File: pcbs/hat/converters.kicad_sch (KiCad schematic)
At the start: 7 parts, among them U18 MCP3008, U19 MCP3008, U20 MCP3008, U21 ???

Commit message: more work on charging circuit
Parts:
- renumbered C25 to C41, C26 to C42, R33 to R65
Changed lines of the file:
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@@
   (symbol (lib_id "power:+5V") (at 90.17 96.52 0) (unit 1)
     (in_bom yes) (on_board yes)
-    (property "Reference" "#PWR0195" (id 0) (at 90.17 100.33 0)
+    (property "Reference" "#PWR0142" (id 0) (at 90.17 100.33 0)
       (effects (font (size 1.27 1.27)) hide)
     )
@@
   (symbol (lib_id "power:GND") (at 86.36 124.46 0) (unit 1)
     (in_bom yes) (on_board yes)
-    (property "Reference" "#PWR0135" (id 0) (at 86.36 130.81 0)
+    (property "Reference" "#PWR0139" (id 0) (at 86.36 130.81 0)
       (effects (font (size 1.27 1.27)) hide)
     )
@@
   (symbol (lib_id "power:+5VA") (at 82.55 52.07 0) (unit 1)
     (in_bom yes) (on_board yes)
-    (property "Reference" "#PWR0159" (id 0) (at 82.55 55.88 0)
+    (property "Reference" "#PWR0135" (id 0) (at 82.55 55.88 0)
       (effects (font (size 1.27 1.27)) hide)
     )
@@
   (symbol (lib_id "power:+5V") (at 90.17 140.97 0) (unit 1)
     (in_bom yes) (on_board yes)
-    (property "Reference" "#PWR0147" (id 0) (at 90.17 144.78 0)
+    (property "Reference" "#PWR0143" (id 0) (at 90.17 144.78 0)
       (effects (font (size 1.27 1.27)) hide)
     )
@@
   (symbol (lib_id "power:GND") (at 86.36 168.91 0) (unit 1)
     (in_bom yes) (on_board yes) (fields_autoplaced)
-    (property "Reference" "#PWR0111" (id 0) (at 86.36 175.26 0)
+    (property "Reference" "#PWR0140" (id 0) (at 86.36 175.26 0)
       (effects (font (size 1.27 1.27)) hide)
     )
@@
   (symbol (lib_id "Device:R") (at 200.025 53.34 90) (unit 1)
     (in_bom yes) (on_board yes) (fields_autoplaced)
-    (property "Reference" "R33" (id 0) (at 200.025 46.99 90))
+    (property "Reference" "R65" (id 0) (at 200.025 46.99 90))
     (property "Value" "R" (id 1) (at 200.025 49.53 90))
     (property "Footprint" "" (id 2) (at 200.025 55.118 90)
@@
   (symbol (lib_id "power:GND") (at 86.36 80.01 0) (unit 1)
     (in_bom yes) (on_board yes) (fields_autoplaced)
-    (property "Reference" "#PWR0203" (id 0) (at 86.36 86.36 0)
+    (property "Reference" "#PWR0138" (id 0) (at 86.36 86.36 0)
       (effects (font (size 1.27 1.27)) hide)
     )
@@
   (symbol (lib_id "power:+5VA") (at 82.55 140.97 0) (unit 1)
     (in_bom yes) (on_board yes)
-    (property "Reference" "#PWR0123" (id 0) (at 82.55 144.78 0)
+    (property "Reference" "#PWR0137" (id 0) (at 82.55 144.78 0)
       (effects (font (size 1.27 1.27)) hide)
     )
@@
   (symbol (lib_id "Device:C") (at 210.185 60.96 0) (unit 1)
     (in_bom yes) (on_board yes) (fields_autoplaced)
-    (property "Reference" "C25" (id 0) (at 213.995 59.6899 0)
+    (property "Reference" "C41" (id 0) (at 213.995 59.6899 0)
       (effects (font (size 1.27 1.27)) (justify left))
     )
@@
   (symbol (lib_id "power:+5VA") (at 82.55 96.52 0) (unit 1)
     (in_bom yes) (on_board yes)
-    (property "Reference" "#PWR0183" (id 0) (at 82.55 100.33 0)
+    (property "Reference" "#PWR0136" (id 0) (at 82.55 100.33 0)
       (effects (font (size 1.27 1.27)) hide)
     )
@@
   (symbol (lib_id "power:GND") (at 224.155 69.85 0) (unit 1)
     (in_bom yes) (on_board yes) (fields_autoplaced)
-    (property "Reference" "#PWR0204" (id 0) (at 224.155 76.2 0)
+    (property "Reference" "#PWR0145" (id 0) (at 224.155 76.2 0)
       (effects (font (size 1.27 1.27)) hide)
     )
@@
   (symbol (lib_id "power:+5VA") (at 192.405 53.34 90) (unit 1)
     (in_bom yes) (on_board yes) (fields_autoplaced)
-    (property "Reference" "#PWR0205" (id 0) (at 196.215 53.34 0)
+    (property "Reference" "#PWR0144" (id 0) (at 196.215 53.34 0)
       (effects (font (size 1.27 1.27)) hide)
     )
@@
   (symbol (lib_id "power:+5VA") (at 238.125 50.8 0) (unit 1)
     (in_bom yes) (on_board yes) (fields_autoplaced)
-    (property "Reference" "#PWR0206" (id 0) (at 238.125 54.61 0)
+    (property "Reference" "#PWR0146" (id 0) (at 238.125 54.61 0)
       (effects (font (size 1.27 1.27)) hide)
     )
@@
   (symbol (lib_id "Device:C") (at 238.125 60.96 0) (unit 1)
     (in_bom yes) (on_board yes) (fields_autoplaced)
-    (property "Reference" "C26" (id 0) (at 241.935 59.6899 0)
+    (property "Reference" "C42" (id 0) (at 241.935 59.6899 0)
       (effects (font (size 1.27 1.27)) (justify left))
     )
@@
   (symbol (lib_id "power:+5V") (at 90.17 52.07 0) (unit 1)
     (in_bom yes) (on_board yes)
-    (property "Reference" "#PWR0171" (id 0) (at 90.17 55.88 0)
-      (effects (font (size 1.27 1.27)) hide)
-    )
+    (property "Reference" "#PWR0141" (id 0) (at 90.17 55.88 0)
+      (effects (font (size 1.27 1.27)) hide)
+    )

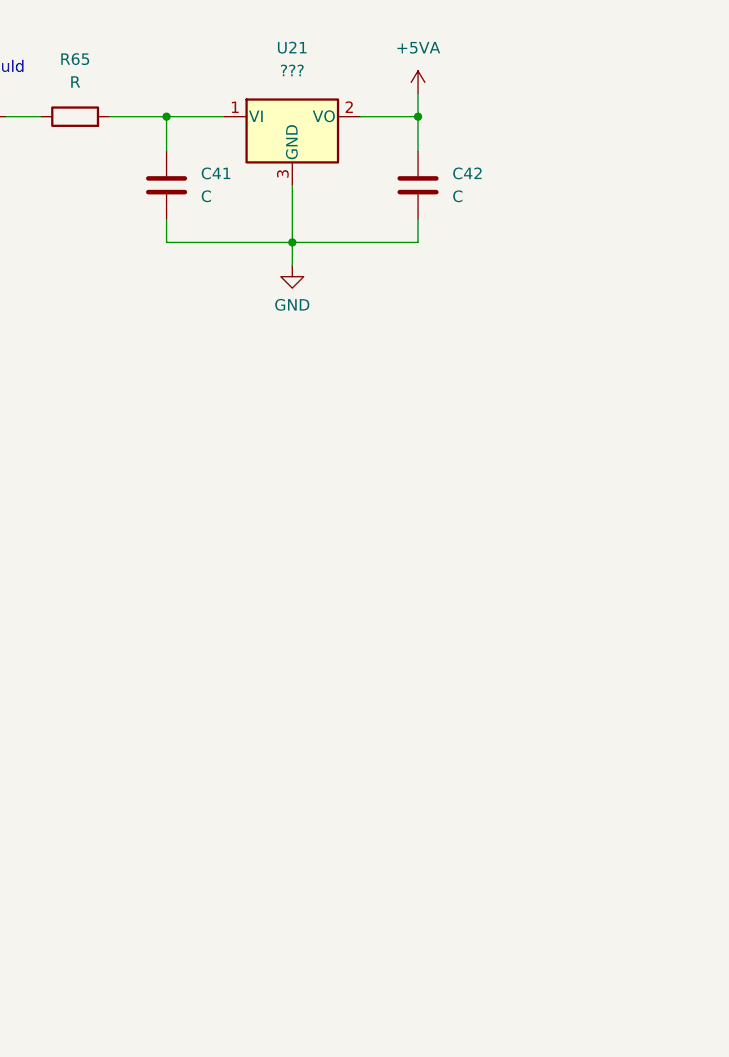
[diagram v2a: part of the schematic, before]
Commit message: fix the current sensor
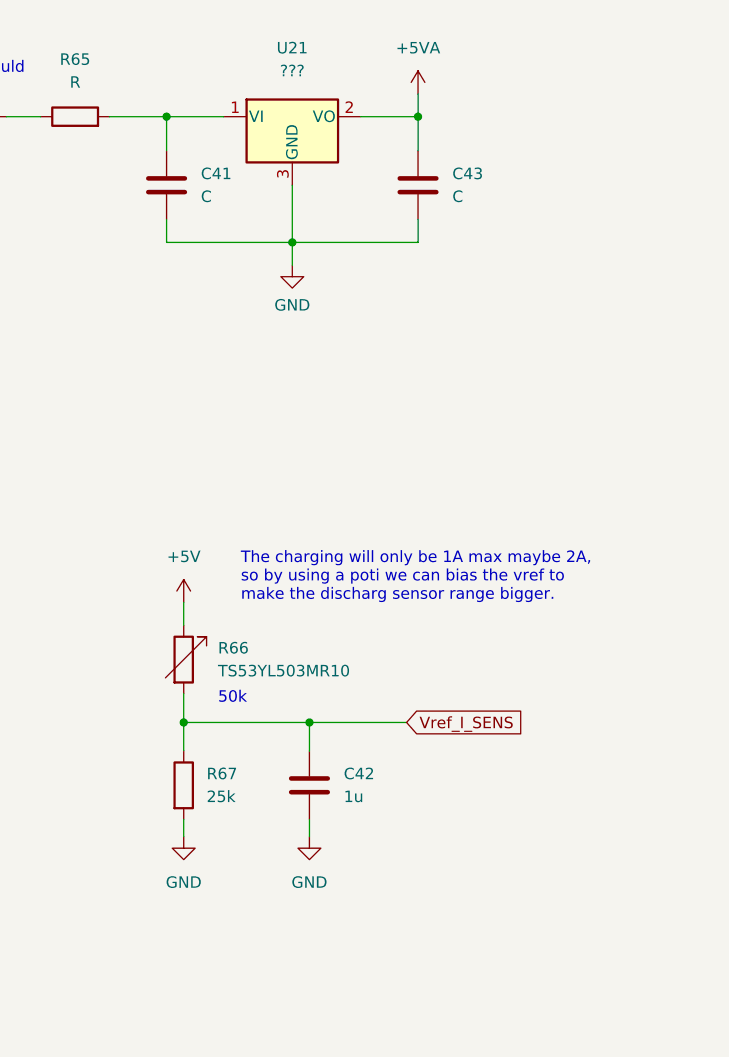
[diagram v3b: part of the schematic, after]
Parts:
- added C42: 1u, Capacitor_SMD:C_0603_1608Metric, symbol Device:C
- added R66: TS53YL503MR10, Potentiometer_SMD:Potentiometer_Vishay_TS53YL_Vertical, symbol Device:R_Variable
- added R67: 25k, Resistor_SMD:R_0805_2012Metric, symbol Device:R
- renumbered C42 to C43
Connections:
- net +5V: now also R66.1
- net GND: now also C42.2, R67.2
- new net Vref_I_SENS: C42.1, R66.2, R67.1
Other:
- note added: "50k"
- note added: "The charging will only be 1A max maybe 2A, so by using a poti we can bias the vref to make the discharg sensor range bigger."
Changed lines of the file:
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@@
   (junction (at 86.36 168.91) (diameter 0) (color 0 0 0 0)
   )
+  (junction (at 226.06 120.65) (diameter 0) (color 0 0 0 0)
+  )
   (junction (at 224.155 67.31) (diameter 0) (color 0 0 0 0)
   )
@@
   (junction (at 238.125 53.34) (diameter 0) (color 0 0 0 0)
   )
+  (junction (at 212.09 120.65) (diameter 0) (color 0 0 0 0)
+  )
   (bus_entry (at 50.8 161.29) (size 2.54 2.54)
     (stroke (width 0) (type default) (color 0 0 0 0))
@@
     (stroke (width 0) (type default) (color 0 0 0 0))
   )
+  (wire (pts (xy 226.06 123.825) (xy 226.06 120.65))
+    (stroke (width 0) (type default) (color 0 0 0 0))
+  )
   (wire (pts (xy 210.185 67.31) (xy 224.155 67.31))
     (stroke (width 0) (type default) (color 0 0 0 0))
@@
     (stroke (width 0) (type default) (color 0 0 0 0))
   )
+  (wire (pts (xy 212.09 131.445) (xy 212.09 133.35))
+    (stroke (width 0) (type default) (color 0 0 0 0))
+  )
   (bus (pts (xy 50.8 143.51) (xy 50.8 146.05))
     (stroke (width 0) (type default) (color 0 0 0 0))
@@
     (stroke (width 0) (type default) (color 0 0 0 0))
   )
+  (wire (pts (xy 212.09 120.65) (xy 212.09 123.825))
+    (stroke (width 0) (type default) (color 0 0 0 0))
+  )
   (wire (pts (xy 231.775 53.34) (xy 238.125 53.34))
     (stroke (width 0) (type default) (color 0 0 0 0))
@@
     (stroke (width 0) (type default) (color 0 0 0 0))
   )
+  (wire (pts (xy 226.06 120.65) (xy 236.855 120.65))
+    (stroke (width 0) (type default) (color 0 0 0 0))
+  )
   (wire (pts (xy 113.03 67.31) (xy 113.03 111.76))
     (stroke (width 0) (type default) (color 0 0 0 0))
@@
     (stroke (width 0) (type default) (color 0 0 0 0))
   )
+  (wire (pts (xy 212.09 107.315) (xy 212.09 109.855))
+    (stroke (width 0) (type default) (color 0 0 0 0))
+  )
   (wire (pts (xy 82.55 80.01) (xy 86.36 80.01))
     (stroke (width 0) (type default) (color 0 0 0 0))
@@
     (stroke (width 0) (type default) (color 0 0 0 0))
   )
+  (wire (pts (xy 226.06 131.445) (xy 226.06 133.35))
+    (stroke (width 0) (type default) (color 0 0 0 0))
+  )
   (wire (pts (xy 53.34 72.39) (xy 69.85 72.39))
     (stroke (width 0) (type default) (color 0 0 0 0))
@@
     (stroke (width 0) (type default) (color 0 0 0 0))
   )
+  (wire (pts (xy 212.09 117.475) (xy 212.09 120.65))
+    (stroke (width 0) (type default) (color 0 0 0 0))
+  )
   (wire (pts (xy 115.57 51.435) (xy 110.49 51.435))
     (stroke (width 0) (type default) (color 0 0 0 0))
@@
     (stroke (width 0) (type default) (color 0 0 0 0))
   )
+  (wire (pts (xy 212.09 120.65) (xy 226.06 120.65))
+    (stroke (width 0) (type default) (color 0 0 0 0))
+  )
   (text "What source should\nwe use here?" (at 177.165 50.8 0)
+    (effects (font (size 1.27 1.27)) (justify left bottom))
+  )
+  (text "50k" (at 215.9 118.745 0)
+    (effects (font (size 1.27 1.27)) (justify left bottom))
+  )
+  (text "The charging will only be 1A max maybe 2A,\nso by using a poti we can bias the vref to\nmake the discharg sensor range bigger."
+    (at 218.44 107.315 0)
     (effects (font (size 1.27 1.27)) (justify left bottom))
   )
@@
     (effects (font (size 1.27 1.27)) (justify left bottom))
   )
+  (global_label "Vref_I_SENS" (shape input) (at 236.855 120.65 0) (fields_autoplaced)
+    (effects (font (size 1.27 1.27)) (justify left))
+    (property "Intersheet References" "${INTERSHEET_REFS}" (id 0) (at 250.3957 120.5706 0)
+      (effects (font (size 1.27 1.27)) (justify left) hide)
+    )
+  )
   (hierarchical_label "SPI_ADC_MISO" (shape bidirectional) (at 115.57 51.435 0)
     (effects (font (size 1.27 1.27)) (justify left))
@@
   (hierarchical_label "SPI_ADC_SCK" (shape input) (at 115.57 48.895 0)
     (effects (font (size 1.27 1.27)) (justify left))
+  )
+  (symbol (lib_id "Device:C") (at 226.06 127.635 0) (unit 1)
+    (in_bom yes) (on_board yes) (fields_autoplaced)
+    (property "Reference" "C42" (id 0) (at 229.87 126.3649 0)
+      (effects (font (size 1.27 1.27)) (justify left))
+    )
+    (property "Value" "1u" (id 1) (at 229.87 128.9049 0)
+      (effects (font (size 1.27 1.27)) (justify left))
+    )
+    (property "Footprint" "Capacitor_SMD:C_0603_1608Metric" (id 2) (at 227.0252 131.445 0)
+      (effects (font (size 1.27 1.27)) hide)
+    )
+    (property "Datasheet" "~" (id 3) (at 226.06 127.635 0)
+      (effects (font (size 1.27 1.27)) hide)
+    )
+    (pin "1")
+    (pin "2")
+  )
+  (symbol (lib_id "Device:R") (at 212.09 127.635 0) (unit 1)
+    (in_bom yes) (on_board yes) (fields_autoplaced)
+    (property "Reference" "R67" (id 0) (at 214.63 126.3649 0)
+      (effects (font (size 1.27 1.27)) (justify left))
+    )
+    (property "Value" "25k" (id 1) (at 214.63 128.9049 0)
+      (effects (font (size 1.27 1.27)) (justify left))
+    )
+    (property "Footprint" "Resistor_SMD:R_0805_2012Metric" (id 2) (at 210.312 127.635 90)
+      (effects (font (size 1.27 1.27)) hide)
+    )
+    (property "Datasheet" "~" (id 3) (at 212.09 127.635 0)
+      (effects (font (size 1.27 1.27)) hide)
+    )
+    (pin "1")
+    (pin "2")
   )
   (symbol (lib_id "power:+5V") (at 90.17 96.52 0) (unit 1)
@@
     )
     (property "Datasheet" "" (id 3) (at 86.36 124.46 0)
+      (effects (font (size 1.27 1.27)) hide)
+    )
+    (pin "1")
+  )
+  (symbol (lib_id "power:GND") (at 212.09 133.35 0) (unit 1)
+    (in_bom yes) (on_board yes) (fields_autoplaced)
+    (property "Reference" "#PWR0146" (id 0) (at 212.09 139.7 0)
+      (effects (font (size 1.27 1.27)) hide)
+    )
+    (property "Value" "GND" (id 1) (at 212.09 138.43 0))
+    (property "Footprint" "" (id 2) (at 212.09 133.35 0)
+      (effects (font (size 1.27 1.27)) hide)
+    )
+    (property "Datasheet" "" (id 3) (at 212.09 133.35 0)
+      (effects (font (size 1.27 1.27)) hide)
+    )
+    (pin "1")
+  )
+  (symbol (lib_id "power:+5V") (at 212.09 107.315 0) (unit 1)
+    (in_bom yes) (on_board yes) (fields_autoplaced)
+    (property "Reference" "#PWR0145" (id 0) (at 212.09 111.125 0)
+      (effects (font (size 1.27 1.27)) hide)
+    )
+    (property "Value" "+5V" (id 1) (at 212.09 102.235 0))
+    (property "Footprint" "" (id 2) (at 212.09 107.315 0)
+      (effects (font (size 1.27 1.27)) hide)
+    )
+    (property "Datasheet" "" (id 3) (at 212.09 107.315 0)
       (effects (font (size 1.27 1.27)) hide)
     )
@@
     (pin "9")
   )
+  (symbol (lib_id "power:GND") (at 226.06 133.35 0) (unit 1)
+    (in_bom yes) (on_board yes) (fields_autoplaced)
+    (property "Reference" "#PWR0148" (id 0) (at 226.06 139.7 0)
+      (effects (font (size 1.27 1.27)) hide)
+    )
+    (property "Value" "GND" (id 1) (at 226.06 138.43 0))
+    (property "Footprint" "" (id 2) (at 226.06 133.35 0)
+      (effects (font (size 1.27 1.27)) hide)
+    )
+    (property "Datasheet" "" (id 3) (at 226.06 133.35 0)
+      (effects (font (size 1.27 1.27)) hide)
+    )
+    (pin "1")
+  )
   (symbol (lib_id "Regulator_Linear:AP7384-70SA") (at 224.155 53.34 0) (unit 1)
     (in_bom yes) (on_board yes) (fields_autoplaced)
@@
     )
     (property "Datasheet" "~" (id 3) (at 200.025 53.34 0)
+      (effects (font (size 1.27 1.27)) hide)
+    )
+    (pin "1")
+    (pin "2")
+  )
+  (symbol (lib_id "Device:R_Variable") (at 212.09 113.665 0) (unit 1)
+    (in_bom yes) (on_board yes) (fields_autoplaced)
+    (property "Reference" "R66" (id 0) (at 215.9 112.3949 0)
+      (effects (font (size 1.27 1.27)) (justify left))
+    )
+    (property "Value" "TS53YL503MR10" (id 1) (at 215.9 114.9349 0)
+      (effects (font (size 1.27 1.27)) (justify left))
+    )
+    (property "Footprint" "Potentiometer_SMD:Potentiometer_Vishay_TS53YL_Vertical" (id 2) (at 210.312 113.665 90)
+      (effects (font (size 1.27 1.27)) hide)
+    )
+    (property "Datasheet" "https://www.mouser.at/datasheet/2/427/ts53-1763731.pdf" (id 3) (at 212.09 113.665 0)
       (effects (font (size 1.27 1.27)) hide)
     )
@@
   (symbol (lib_id "power:GND") (at 224.155 69.85 0) (unit 1)
     (in_bom yes) (on_board yes) (fields_autoplaced)
-    (property "Reference" "#PWR0145" (id 0) (at 224.155 76.2 0)
+    (property "Reference" "#PWR0147" (id 0) (at 224.155 76.2 0)
       (effects (font (size 1.27 1.27)) hide)
     )
@@
   (symbol (lib_id "power:+5VA") (at 238.125 50.8 0) (unit 1)
     (in_bom yes) (on_board yes) (fields_autoplaced)
-    (property "Reference" "#PWR0146" (id 0) (at 238.125 54.61 0)
+    (property "Reference" "#PWR0149" (id 0) (at 238.125 54.61 0)
       (effects (font (size 1.27 1.27)) hide)
     )
@@
   (symbol (lib_id "Device:C") (at 238.125 60.96 0) (unit 1)
     (in_bom yes) (on_board yes) (fields_autoplaced)
-    (property "Reference" "C42" (id 0) (at 241.935 59.6899 0)
-      (effects (font (size 1.27 1.27)) (justify left))
-    )
+    (property "Reference" "C43" (id 0) (at 241.935 59.6899 0)
+      (effects (font (size 1.27 1.27)) (justify left))
+    )

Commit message: change ADCs and connect all Sensors and Signals
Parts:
- removed U18, U19, U20: MCP3008, Package_SO:SOIC-16_3.9x9.9mm_P1.27mm, symbol Analog_ADC:MCP3008
- added U18, U19, U20: ADS7828, Package_SO:TSSOP-16_4.4x5mm_P0.65mm, symbol Analog_ADC:ADS7828
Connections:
- net +5V: now also R65.1, U18.16 (VDD), U19.12 (A0), U19.16 (VDD), U20.13 (A1), U20.16 (VDD)
- net +5VA: now also U18.10 (REF), U19.10 (REF), U20.10 (REF); no longer R65.1
- net GND: now also U18.11 (COM), U18.12 (A0), U18.13 (A1), U18.9 (GND), U19.11 (COM), U19.13 (A1), U19.9 (GND), U20.11 (COM), U20.12 (A0), U20.9 (GND)
- net SENSOR_10: now also U18.1 (CH0)
- net SENSOR_11: now also U19.1 (CH0)
- net SENSOR_12: now also U20.1 (CH0)
- net SENSOR_20: now also U18.2 (CH1)
- net SENSOR_21: now also U19.2 (CH1)
- net SENSOR_22: now also U20.2 (CH1)
- net SENSOR_30: now also U18.3 (CH2)
- net SENSOR_31: now also U19.3 (CH2)
- net SENSOR_32: now also U20.3 (CH2)
- net SENSOR_40: now also U18.4 (CH3)
- net SENSOR_41: now also U19.4 (CH3)
- net SENSOR_42: now also U20.4 (CH3)
- net SENSOR_50: now also U18.5 (CH4)
- net SENSOR_51: now also U19.5 (CH4)
- net SENSOR_52: now also U20.5 (CH4)
- net SENSOR_60: now also U18.6 (CH5)
- net SENSOR_61: now also U19.6 (CH5)
- net SENSOR_62: now also U20.6 (CH5)
- net SENSOR_70: now also U18.7 (CH6)
- net SENSOR_71: now also U19.7 (CH6)
- net SENSOR_72: now also U20.7 (CH6)
- net SENSOR_80: now also U18.8 (CH7)
- net SENSOR_81: now also U19.8 (CH7)
- net SENSOR_82: now also U20.8 (CH7)
- new net SCL: U18.14 (SCL), U19.14 (SCL), U20.14 (SCL)
- new net SDA: U18.15 (SDA), U19.15 (SDA), U20.15 (SDA)
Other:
- note added: "Addr 0"
- note added: "Addr 1"
- note added: "Addr 2"

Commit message: formatting
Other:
- note added: "ADCs"
- note added: "V_{ref} Voltage Amplifiers"
- moved on the sheet: C41, C42, C43, R65, R66, R67, U18, U19, U20, U21
